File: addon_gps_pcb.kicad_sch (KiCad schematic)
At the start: 7 parts, among them J11 WS2812B, U9 SAM-M10Q

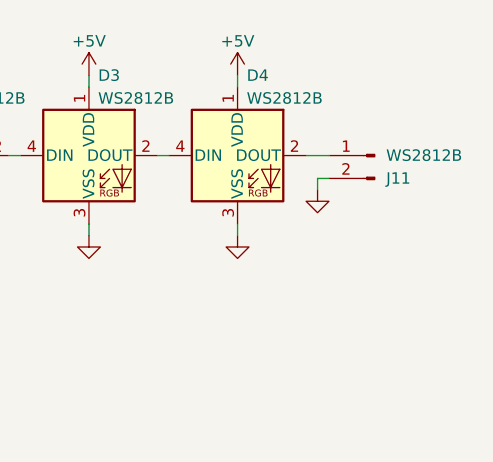
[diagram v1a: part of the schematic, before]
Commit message: Add schematic changes from PCB routing/layout
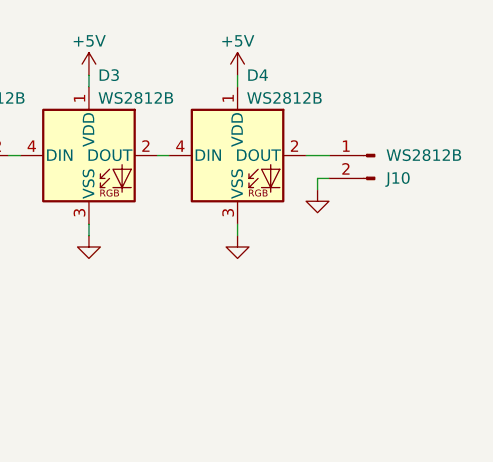
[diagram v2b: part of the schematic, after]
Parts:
- renumbered J11 to J10
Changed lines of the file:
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@@
 		(on_board yes)
 		(dnp no)
-		(property "Reference" "#PWR074"
+		(property "Reference" "#PWR072"
 			(at 194.31 25.4 0)
 			(effects
@@
 			(project "nerve_pcb"
 				(path "/c0277862-b3f2-4e0e-986f-34702f0543f0/5e5db2cb-8fc9-48f2-985b-a0cd6e1a3554"
-					(reference "#PWR074")
+					(reference "#PWR072")
 					(unit 1)
 				)
@@
 		(on_board yes)
 		(dnp no)
-		(property "Reference" "J11"
+		(property "Reference" "J10"
 			(at 210.82 33.0201 0)
 			(effects
@@
 			(project "nerve_pcb"
 				(path "/c0277862-b3f2-4e0e-986f-34702f0543f0/5e5db2cb-8fc9-48f2-985b-a0cd6e1a3554"
-					(reference "J11")
+					(reference "J10")
 					(unit 1)
 				)
@@
 		(dnp no)
 		(fields_autoplaced yes)
-		(property "Reference" "#PWR079"
+		(property "Reference" "#PWR077"
 			(at 161.29 45.72 0)
 			(effects
@@
 			(project "nerve_pcb"
 				(path "/c0277862-b3f2-4e0e-986f-34702f0543f0/5e5db2cb-8fc9-48f2-985b-a0cd6e1a3554"
-					(reference "#PWR079")
+					(reference "#PWR077")
 					(unit 1)
 				)
@@
 		(on_board yes)
 		(dnp no)
-		(property "Reference" "#PWR069"
+		(property "Reference" "#PWR067"
 			(at 53.34 24.13 0)
 			(effects
@@
 			(project "nerve_pcb"
 				(path "/c0277862-b3f2-4e0e-986f-34702f0543f0/5e5db2cb-8fc9-48f2-985b-a0cd6e1a3554"
-					(reference "#PWR069")
+					(reference "#PWR067")
 					(unit 1)
 				)
@@
 		(dnp no)
 		(fields_autoplaced yes)
-		(property "Reference" "#PWR077"
+		(property "Reference" "#PWR075"
 			(at 91.44 45.72 0)
 			(effects
@@
 			(project "nerve_pcb"
 				(path "/c0277862-b3f2-4e0e-986f-34702f0543f0/5e5db2cb-8fc9-48f2-985b-a0cd6e1a3554"
-					(reference "#PWR077")
+					(reference "#PWR075")
 					(unit 1)
 				)
@@
 		(dnp no)
 		(fields_autoplaced yes)
-		(property "Reference" "#PWR080"
+		(property "Reference" "#PWR078"
 			(at 177.8 45.72 0)
 			(effects
@@
 			(project "nerve_pcb"
 				(path "/c0277862-b3f2-4e0e-986f-34702f0543f0/5e5db2cb-8fc9-48f2-985b-a0cd6e1a3554"
-					(reference "#PWR080")
+					(reference "#PWR078")
 					(unit 1)
 				)
@@
 		(on_board yes)
 		(dnp no)
-		(property "Reference" "#PWR075"
+		(property "Reference" "#PWR073"
 			(at 104.14 35.56 0)
 			(effects
@@
 			(project "nerve_pcb"
 				(path "/c0277862-b3f2-4e0e-986f-34702f0543f0/5e5db2cb-8fc9-48f2-985b-a0cd6e1a3554"
-					(reference "#PWR075")
+					(reference "#PWR073")
 					(unit 1)
 				)
@@
 		(dnp no)
 		(fields_autoplaced yes)
-		(property "Reference" "#PWR078"
+		(property "Reference" "#PWR076"
 			(at 144.78 45.72 0)
 			(effects
@@
 			(project "nerve_pcb"
 				(path "/c0277862-b3f2-4e0e-986f-34702f0543f0/5e5db2cb-8fc9-48f2-985b-a0cd6e1a3554"
-					(reference "#PWR078")
+					(reference "#PWR076")
 					(unit 1)
 				)
@@
 		(dnp no)
 		(fields_autoplaced yes)
-		(property "Reference" "#PWR081"
+		(property "Reference" "#PWR079"
 			(at 194.31 45.72 0)
 			(effects
@@
 			(project "nerve_pcb"
 				(path "/c0277862-b3f2-4e0e-986f-34702f0543f0/5e5db2cb-8fc9-48f2-985b-a0cd6e1a3554"
-					(reference "#PWR081")
+					(reference "#PWR079")
 					(unit 1)
 				)
@@
 		(dnp no)
 		(fields_autoplaced yes)
-		(property "Reference" "#PWR076"
+		(property "Reference" "#PWR074"
 			(at 203.2 40.64 0)
 			(effects
@@
 			(project "nerve_pcb"
 				(path "/c0277862-b3f2-4e0e-986f-34702f0543f0/5e5db2cb-8fc9-48f2-985b-a0cd6e1a3554"
-					(reference "#PWR076")
+					(reference "#PWR074")
 					(unit 1)
 				)
@@
 		(on_board yes)
 		(dnp no)
-		(property "Reference" "#PWR070"
+		(property "Reference" "#PWR068"
 			(at 48.26 25.4 0)
 			(effects
@@
 			(project "nerve_pcb"
 				(path "/c0277862-b3f2-4e0e-986f-34702f0543f0/5e5db2cb-8fc9-48f2-985b-a0cd6e1a3554"
-					(reference "#PWR070")
+					(reference "#PWR068")
 					(unit 1)
 				)
@@
 		(on_board yes)
 		(dnp no)
-		(property "Reference" "#PWR072"
+		(property "Reference" "#PWR070"
 			(at 161.29 25.4 0)
 			(effects
@@
 			(project "nerve_pcb"
 				(path "/c0277862-b3f2-4e0e-986f-34702f0543f0/5e5db2cb-8fc9-48f2-985b-a0cd6e1a3554"
-					(reference "#PWR072")
+					(reference "#PWR070")
 					(unit 1)
 				)
@@
 		(on_board yes)
 		(dnp no)
-		(property "Reference" "#PWR071"
+		(property "Reference" "#PWR069"
 			(at 144.78 25.4 0)
 			(effects
@@
 			(project "nerve_pcb"
 				(path "/c0277862-b3f2-4e0e-986f-34702f0543f0/5e5db2cb-8fc9-48f2-985b-a0cd6e1a3554"
-					(reference "#PWR071")
+					(reference "#PWR069")
 					(unit 1)
 				)
@@
 		(dnp no)
 		(fields_autoplaced yes)
-		(property "Reference" "#PWR082"
+		(property "Reference" "#PWR080"
 			(at 63.5 67.31 0)
 			(effects
@@
 			(project "nerve_pcb"
 				(path "/c0277862-b3f2-4e0e-986f-34702f0543f0/5e5db2cb-8fc9-48f2-985b-a0cd6e1a3554"
-					(reference "#PWR082")
+					(reference "#PWR080")
 					(unit 1)
 				)
@@
 		(on_board yes)
 		(dnp no)
-		(property "Reference" "#PWR073"
+		(property "Reference" "#PWR071"
 			(at 177.8 25.4 0)
 			(effects
@@
 			(project "nerve_pcb"
 				(path "/c0277862-b3f2-4e0e-986f-34702f0543f0/5e5db2cb-8fc9-48f2-985b-a0cd6e1a3554"
-					(reference "#PWR073")
-					(unit 1)
-				)
+					(reference "#PWR071")
+					(unit 1)
+				)

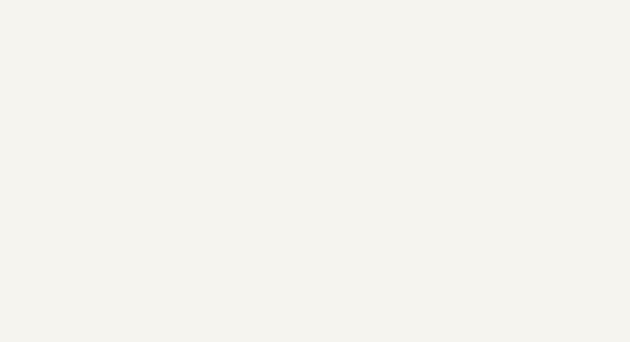
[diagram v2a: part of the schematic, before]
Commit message: Add mounting holes to secondary schematics
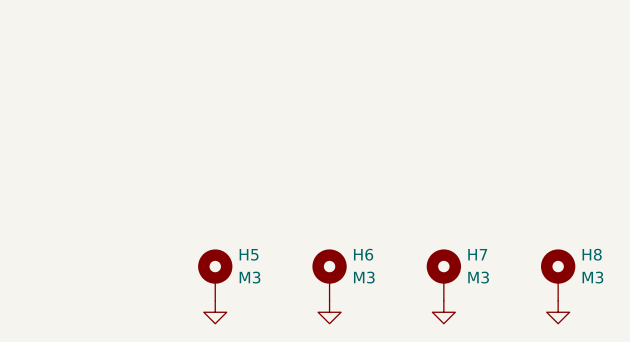
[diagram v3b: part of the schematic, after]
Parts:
- added H5, H6, H7, H8: M3, MountingHole:MountingHole_3.2mm_M3_Pad_Via, symbol Mechanical:MountingHole_Pad
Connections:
- net GND: now also H5.1, H6.1, H7.1, H8.1

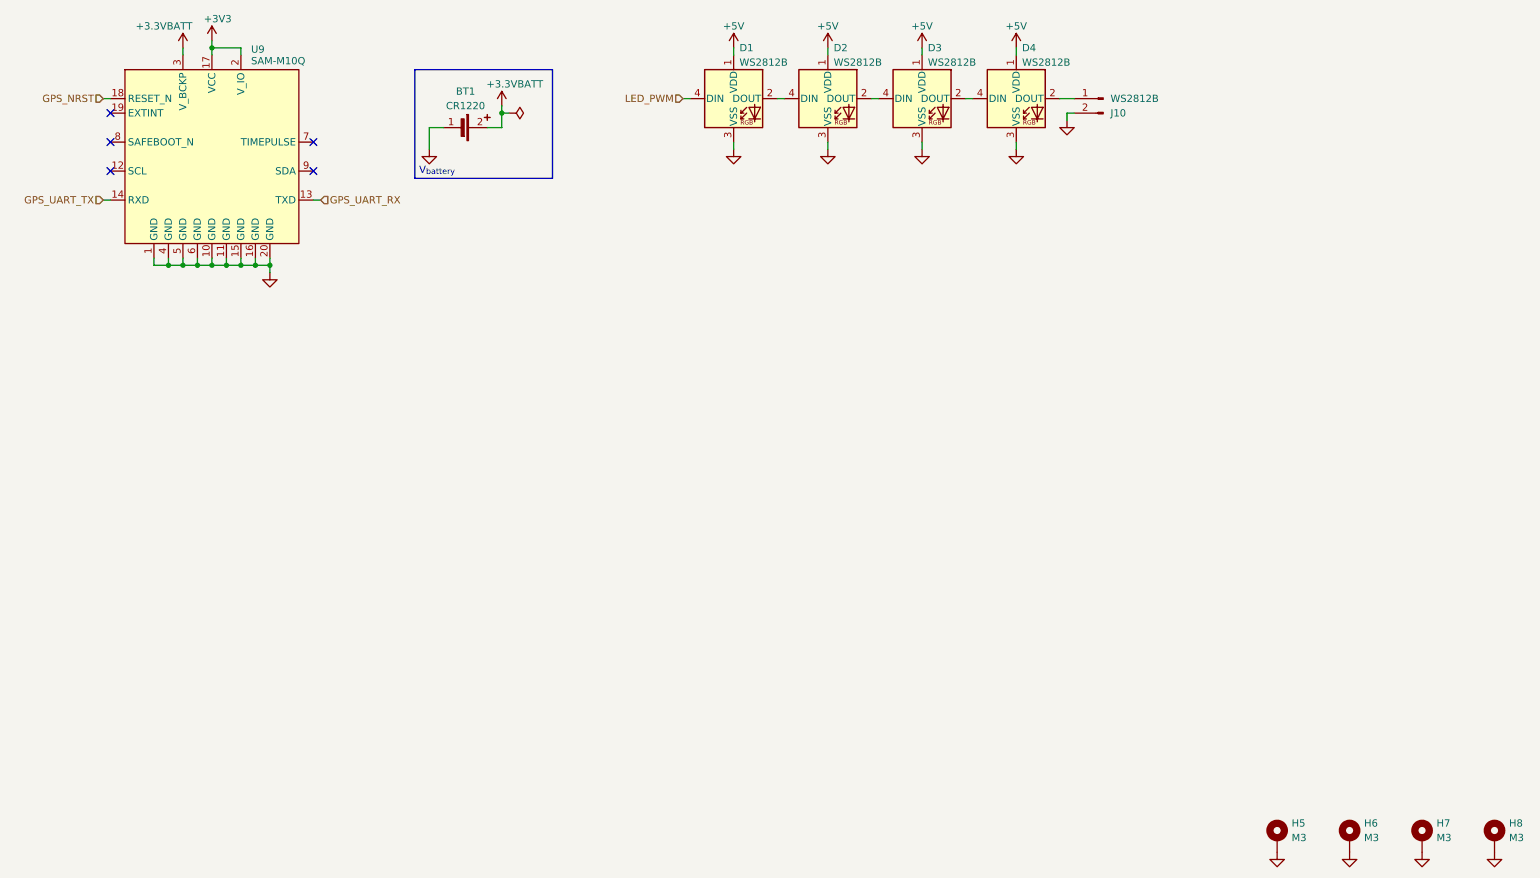
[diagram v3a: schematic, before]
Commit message: Update schematics for add-on PCB separation
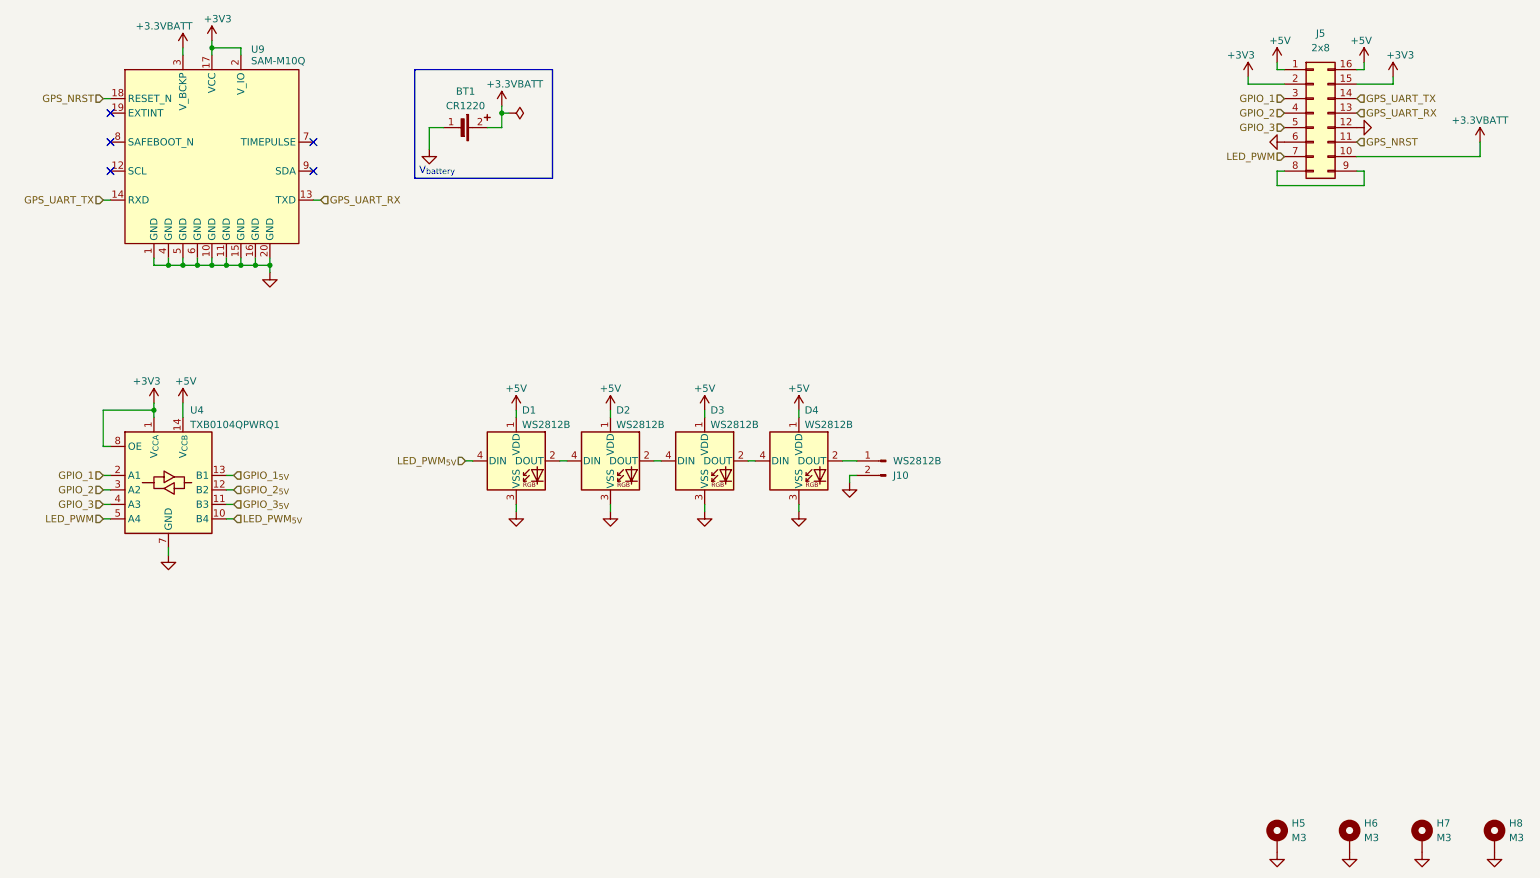
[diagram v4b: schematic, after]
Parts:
- added J5: 2x8, symbol Connector_Generic:Conn_02x08_Counter_Clockwise
- added U4: TXB0104QPWRQ1, common:txb0104qpwrq1, symbol common:txb0104qpwrq1
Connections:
- net +3.3VBATT: now also J5.10 (Pin_10)
- net +3V3: now also J5.15 (Pin_15), J5.2 (Pin_2), U4.1 (V_{CCA}), U4.8 (OE)
- net +5V: now also J5.1 (Pin_1), J5.16 (Pin_16), U4.14 (V_{CCB})
- net GND: now also J5.12 (Pin_12), J5.6 (Pin_6), U4.7 (GND)
- net GPS_NRST: now also J5.11 (Pin_11)
- net GPS_UART_RX: now also J5.13 (Pin_13)
- net GPS_UART_TX: now also J5.14 (Pin_14)
- net LED_PWM: now also J5.7 (Pin_7), U4.5 (A4); no longer D1.4 (DIN)
- new net: J5.8 (Pin_8), J5.9 (Pin_9)
- new net GPIO_1: J5.3 (Pin_3), U4.2 (A1)
- new net GPIO_1_{5V}: U4.13 (B1)
- new net GPIO_2: J5.4 (Pin_4), U4.3 (A2)
- new net GPIO_2_{5V}: U4.12 (B2)
- new net GPIO_3: J5.5 (Pin_5), U4.4 (A3)
- new net GPIO_3_{5V}: U4.11 (B3)
- new net LED_PWM_{5V}: D1.4 (DIN), U4.10 (B4)
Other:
- moved on the sheet: D1, D2, D3, D4, J10

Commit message: Update refs on schematics
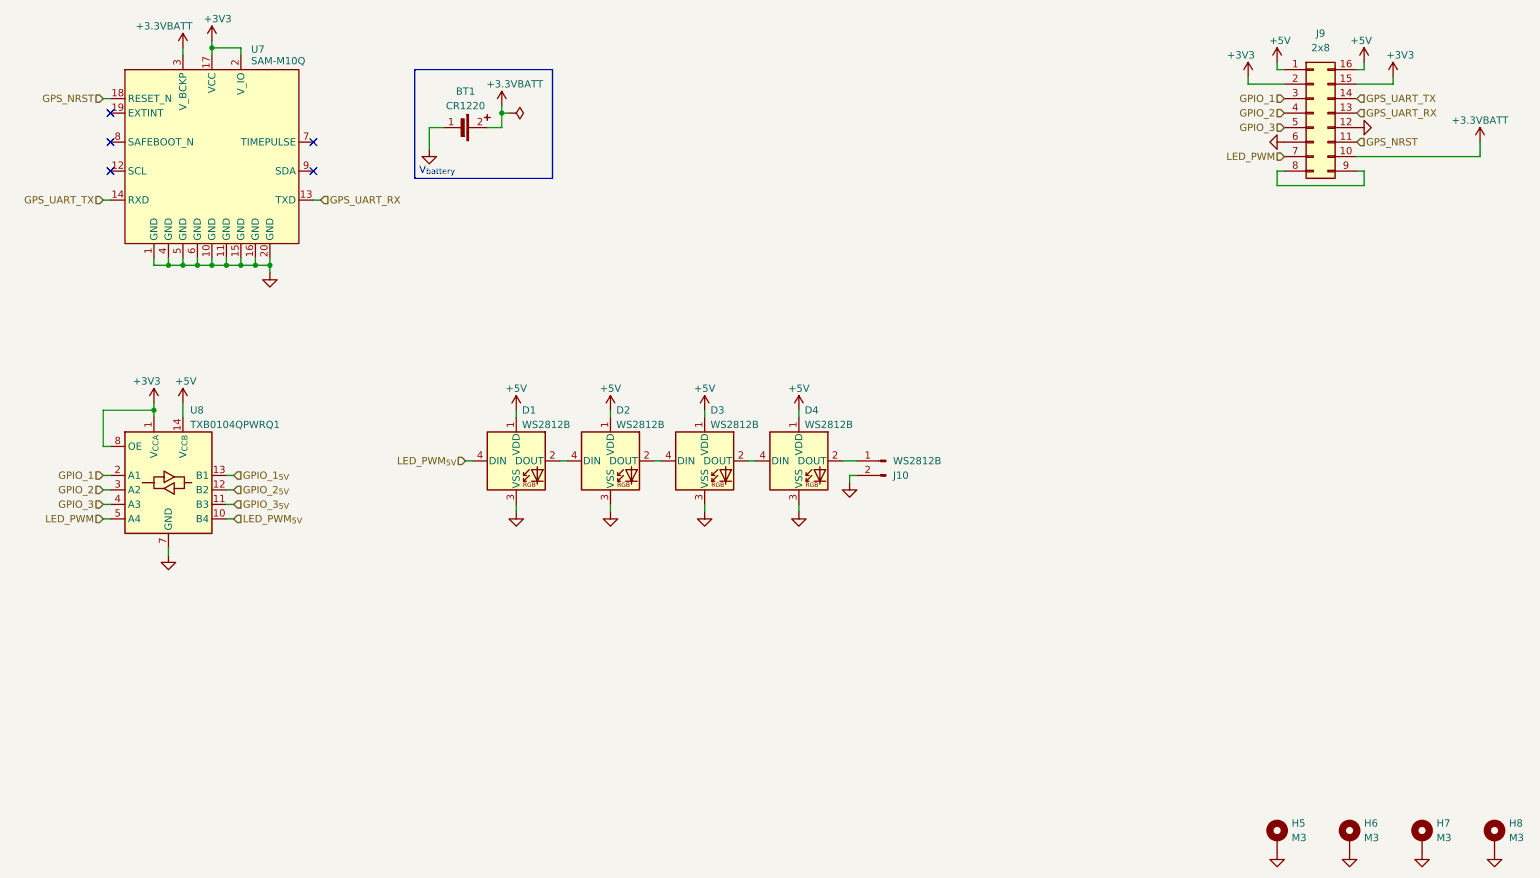
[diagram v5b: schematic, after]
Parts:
- renumbered J5 to J9, U9 to U7, U4 to U8

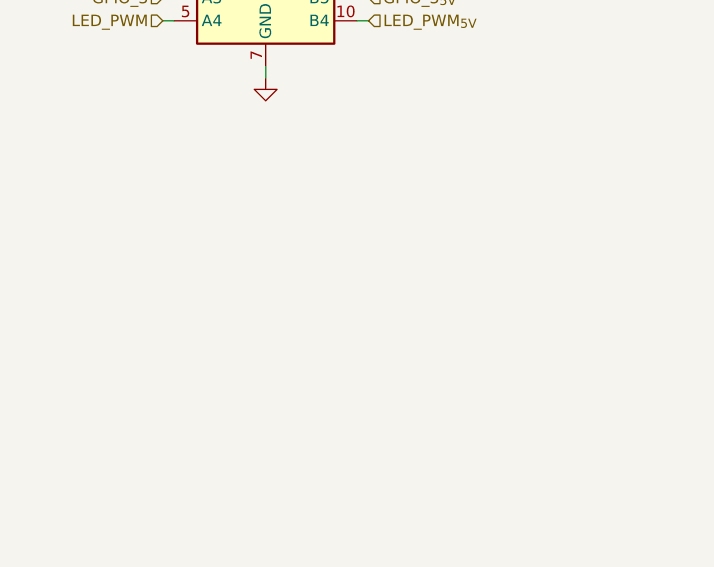
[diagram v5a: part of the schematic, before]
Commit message: Add breakout connectors to add-on PCBs
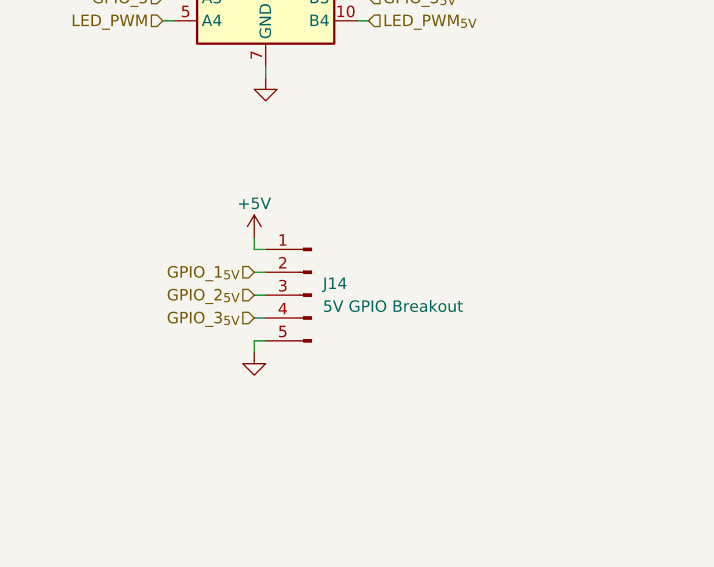
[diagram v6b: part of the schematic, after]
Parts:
- added J14: 5V GPIO Breakout, symbol Connector:Conn_01x05_Pin
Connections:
- net +5V: now also J14.1 (Pin_1)
- net GND: now also J14.5 (Pin_5)
- net GPIO_1_{5V}: now also J14.2 (Pin_2)
- net GPIO_2_{5V}: now also J14.3 (Pin_3)
- net GPIO_3_{5V}: now also J14.4 (Pin_4)
